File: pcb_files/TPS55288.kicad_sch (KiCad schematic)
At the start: 35 parts, among them Q6 CSD18513Q5A, Q7 CSD18513Q5A, U10 TPS55288RPMR

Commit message: Changed TPS55288 to internal droop compensation and added current monitoring for TPS55288 to ADC pin of LicheeRV Nano
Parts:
- removed C128: 4.7nF, Capacitor_SMD:C_0402_1005Metric, symbol JLCImport:CGA0402X7R472K250GT
- removed C134: 100nF, Capacitor_SMD:C_0402_1005Metric, symbol JLCImport:CL05B104KB54PNC
- removed R89: 56.2k, Resistor_SMD:R_0402_1005Metric, symbol JLCImport:0402WGF5622TCE
- removed R90: 42.2k, Resistor_SMD:R_0402_1005Metric, symbol JLCImport:CR0402F42K2Q10Z
- removed R91: 150k, Resistor_SMD:R_0603_1608Metric, symbol JLCImport:0603WAF1503T5E
- added C117: 10nF, Capacitor_SMD:C_0402_1005Metric, symbol JLCImport:TCC0402X7R103M500AT
- added C118: 4.7nF, Capacitor_SMD:C_0402_1005Metric, symbol JLCImport:TCC0402X7R472K500AT
- added R78: 56.2k, Resistor_SMD:R_0402_1005Metric, symbol JLCImport:CR0402FF5622G
- added R80: 20k, Resistor_SMD:R_0402_1005Metric, symbol JLCImport:CR0402J20K0Q10Z
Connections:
- net AGND: now also C117.1, C118.1, R80.1
- net I_MONITOR: now reaches U10.16 (CDC)
- net at U10.17 (ILIM): now also R80.2
- net at C127.2, U10.18 (COMP): now also R78.2
- net at U10.7 (DITH/SYNC): now also C117.2
- new net: C118.2, R78.1

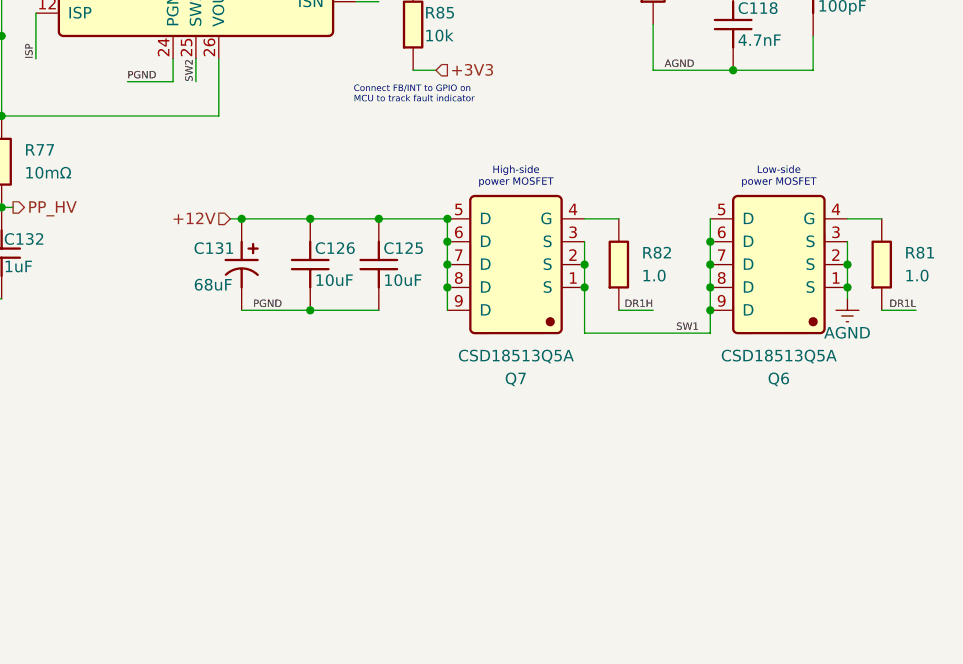
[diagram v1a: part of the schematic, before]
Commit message: Basic Function Review/Documentation for TPS55288
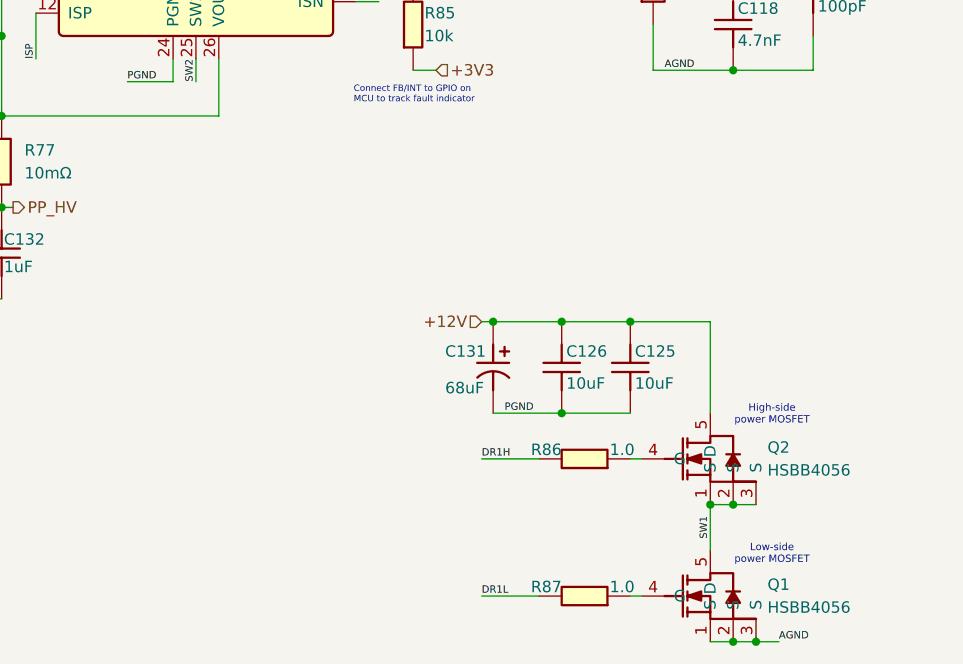
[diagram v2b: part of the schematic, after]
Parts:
- removed Q6, Q7: CSD18513Q5A, JLCImport:CSD18513Q5A, symbol JLCImport:CSD18513Q5A
- removed R81, R82: 1.0, Resistor_SMD:R_0402_1005Metric, symbol JLCImport:WR04W1R00FTL
- added Q1, Q2: HSBB4056, JLCImport:HSBB4056, symbol JLCImport:HSBB4056
- added R86, R87: 1.0, Resistor_SMD:R_0402_1005Metric, symbol JLCImport:WR04W1R00FTL
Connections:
- net +12V: now also Q2.5 (D)
- net DR1H: now also R86.2
- net DR1L: now also R87.2
- net SW1: now also Q1.5 (D), Q2.1 (S), Q2.2 (S), Q2.3 (S)
- net AGND renamed GND
- net GND: now also Q1.1 (S), Q1.2 (S), Q1.3 (S)
- new net: Q2.4 (G), R86.1
- new net: Q1.4 (G), R87.1

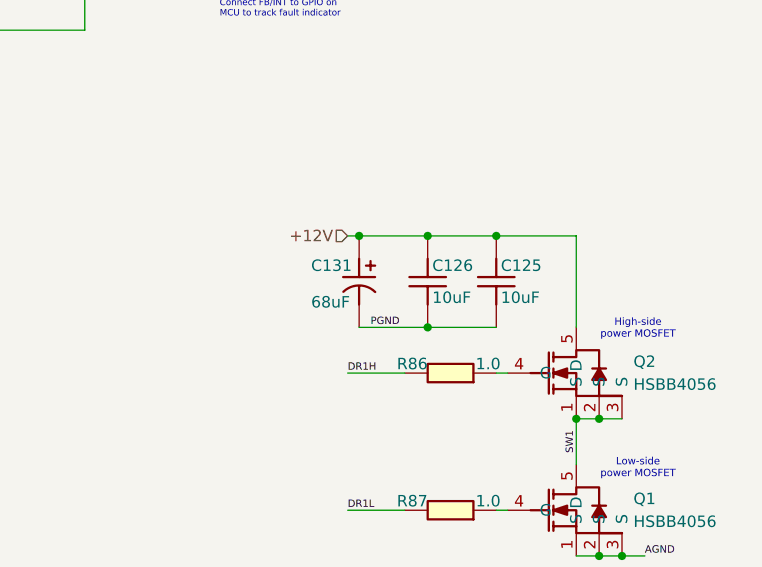
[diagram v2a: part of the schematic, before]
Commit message: Basic Function Review/Documentation for MCP9808
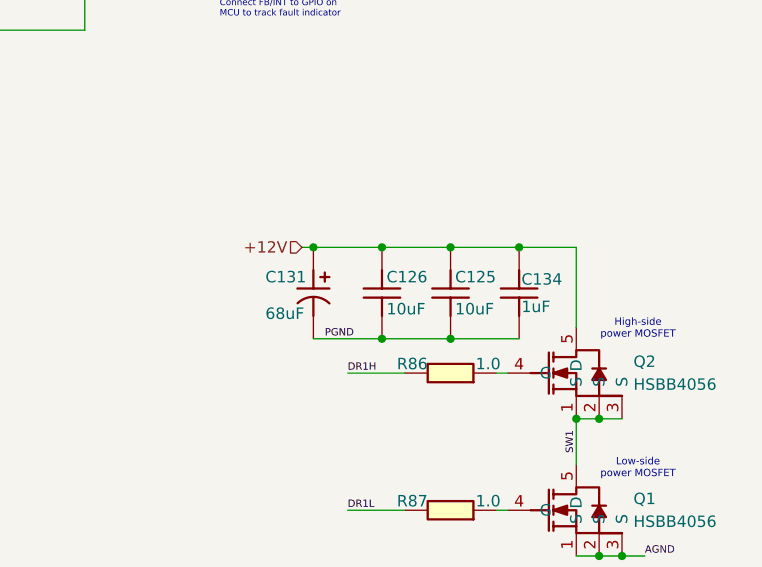
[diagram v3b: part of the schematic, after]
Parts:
- added C134: 1uF, Capacitor_SMD:C_0402_1005Metric, symbol JLCImport:CL05A105KA5NQNC
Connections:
- net +12V: now also C134.2
- net GND: now also C134.1
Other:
- moved on the sheet: C125, C126, C131
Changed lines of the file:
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@@
 	)
 	(junction
-		(at 154.94 109.22)
+		(at 149.86 110.49)
 		(diameter 0)
-		(color 0 0 0 0)
+		(color 139 0 0 1)
 	)
 	(junction
@@
 	)
 	(junction
-		(at 154.94 99.06)
+		(at 149.86 100.33)
 		(diameter 0)
 		(color 0 0 0 0)
@@
 	)
 	(junction
+		(at 157.48 110.49)
+		(diameter 0)
+		(color 139 0 0 1)
+	)
+	(junction
 		(at 60.96 57.15)
 		(diameter 0)
@@
 	)
 	(junction
-		(at 162.56 99.06)
+		(at 157.48 100.33)
 		(diameter 0)
 		(color 0 0 0 0)
@@
 	)
 	(junction
+		(at 165.1 100.33)
+		(diameter 0)
+		(color 0 0 0 0)
+	)
+	(junction
 		(at 74.93 53.34)
 		(diameter 0)
@@
 	)
 	(junction
-		(at 147.32 99.06)
+		(at 142.24 100.33)
 		(diameter 0)
 		(color 0 0 0 0)
@@
 	(wire
 		(pts
-			(xy 147.32 99.06) (xy 154.94 99.06)
+			(xy 142.24 100.33) (xy 149.86 100.33)
 		)
 		(stroke
@@
 	(wire
 		(pts
+			(xy 157.48 110.49) (xy 165.1 110.49)
+		)
+		(stroke
+			(width 0)
+			(type default)
+			(color 139 0 0 1)
+		)
+	)
+	(wire
+		(pts
 			(xy 149.86 40.64) (xy 151.13 40.64)
 		)
@@
 	(wire
 		(pts
-			(xy 74.93 53.34) (xy 74.93 52.07)
+			(xy 171.45 100.33) (xy 171.45 109.22)
 		)
 		(stroke
 			(width 0)
 			(type default)
-			(color 139 0 0 1)
 		)
 	)
 	(wire
 		(pts
-			(xy 31.75 58.42) (xy 31.75 57.15)
+			(xy 74.93 53.34) (xy 74.93 52.07)
 		)
 		(stroke
@@
 	(wire
 		(pts
-			(xy 165.1 71.12) (xy 173.99 71.12)
+			(xy 31.75 58.42) (xy 31.75 57.15)
 		)
 		(stroke
@@
 	(wire
 		(pts
-			(xy 171.45 109.22) (xy 171.45 99.06)
+			(xy 165.1 71.12) (xy 173.99 71.12)
 		)
 		(stroke
 			(width 0)
 			(type default)
+			(color 139 0 0 1)
 		)
 	)
@@
 	(wire
 		(pts
-			(xy 154.94 109.22) (xy 162.56 109.22)
+			(xy 149.86 110.49) (xy 157.48 110.49)
 		)
 		(stroke
@@
 	(wire
 		(pts
+			(xy 165.1 100.33) (xy 171.45 100.33)
+		)
+		(stroke
+			(width 0)
+			(type default)
+		)
+	)
+	(wire
+		(pts
 			(xy 173.99 134.62) (xy 176.53 134.62)
 		)
@@
 	(wire
 		(pts
-			(xy 162.56 99.06) (xy 171.45 99.06)
+			(xy 157.48 100.33) (xy 165.1 100.33)
 		)
 		(stroke
@@
 	(wire
 		(pts
-			(xy 147.32 109.22) (xy 154.94 109.22)
+			(xy 142.24 110.49) (xy 149.86 110.49)
 		)
 		(stroke
@@
 	(wire
 		(pts
-			(xy 154.94 99.06) (xy 162.56 99.06)
+			(xy 149.86 100.33) (xy 157.48 100.33)
 		)
 		(stroke
@@
 	(wire
 		(pts
-			(xy 146.05 99.06) (xy 147.32 99.06)
+			(xy 140.97 100.33) (xy 142.24 100.33)
 		)
 		(stroke
@@
 	)
 	(label "PGND"
-		(at 148.59 109.22 0)
+		(at 143.51 110.49 0)
 		(effects
 			(font
@@
 	(hierarchical_label "+12V"
 		(shape input)
-		(at 146.05 99.06 180)
+		(at 140.97 100.33 180)
 		(effects
 			(font
@@
 	(symbol
 		(lib_id "JLCImport:DHG100M686G150S1AA")
-		(at 147.32 104.14 270)
+		(at 142.24 105.41 270)
 		(unit 1)
 		(body_style 1)
@@
 		(dnp no)
 		(property "Reference" "C131"
-			(at 141.986 102.362 90)
+			(at 136.906 103.632 90)
 			(show_name no)
 			(do_not_autoplace no)
@@
 		)
 		(property "Value" "68uF"
-			(at 141.986 106.426 90)
+			(at 136.906 107.696 90)
 			(show_name no)
 			(do_not_autoplace no)
@@
 		)
 		(property "Footprint" "JLCImport:DHG100M686G150S1AA"
-			(at 147.32 104.14 0)
+			(at 142.24 105.41 0)
 			(hide yes)
 			(show_name no)
@@
 		)
 		(property "Datasheet" "https://atta.szlcsc.com/upload/public/pdf/source/20250828/0654BD1517550F7FB040F38784C4EB35.pdf"
-			(at 147.32 104.14 0)
+			(at 142.24 105.41 0)
 			(hide yes)
 			(show_name no)
@@
 		)
 		(property "Description" "68uF ±20% 100V"
-			(at 147.32 104.14 0)
+			(at 142.24 105.41 0)
 			(hide yes)
 			(show_name no)
@@
 		)
 		(property "LCSC" "C46551229"
-			(at 147.32 104.14 0)
+			(at 142.24 105.41 0)
 			(hide yes)
 			(show_name no)
@@
 		)
 		(property "Manufacturer" "KNSCHA(科尼盛)"
-			(at 147.32 104.14 0)
+			(at 142.24 105.41 0)
 			(hide yes)
 			(show_name no)
@@
 		)
 		(property "Manufacturer Part" "DHG100M686G150S1AA"
-			(at 147.32 104.14 0)
+			(at 142.24 105.41 0)
 			(hide yes)
 			(show_name no)
@@
 		(lib_name "CL21A106KAYNNNE_1")
 		(lib_id "JLCImport:CL21A106KAYNNNE")
-		(at 162.56 104.14 90)
+		(at 157.48 105.41 90)
 		(unit 1)
 		(body_style 1)
@@
 		(dnp no)
 		(property "Reference" "C125"
-			(at 163.068 102.362 90)
+			(at 157.988 103.632 90)
 			(show_name no)
 			(do_not_autoplace no)
@@
 		)
 		(property "Value" "10uF"
-			(at 163.068 105.918 90)
+			(at 157.988 107.188 90)
 			(show_name no)
 			(do_not_autoplace no)
@@
 		)
 		(property "Footprint" "Capacitor_SMD:C_0805_2012Metric"
-			(at 162.56 104.14 0)
+			(at 157.48 105.41 0)
 			(hide yes)
 			(show_name no)
@@
 		)
 		(property "Datasheet" "https://www.lcsc.com/datasheet/lcsc_datasheet_2304140030_Samsung-Electro-Mechanics-CL21A106KAYNNNE_C15850.pdf"
-			(at 162.56 104.14 0)
+			(at 157.48 105.41 0)
 			(hide yes)
 			(show_name no)
@@
 		)
 		(property "Description" "10uF 25V X5R ±10% 0805 Multilayer Ceramic Capacitors MLCC - SMD/SMT ROHS"
-			(at 162.56 104.14 0)
+			(at 157.48 105.41 0)
 			(hide yes)
 			(show_name no)
@@
 		)
 		(property "LCSC" "C15850"
-			(at 162.56 104.14 0)
+			(at 157.48 105.41 0)
 			(hide yes)
 			(show_name no)
@@
 		)
 		(property "Manufacturer" "Samsung Electro-Mechanics"
-			(at 162.56 104.14 0)
+			(at 157.48 105.41 0)
 			(hide yes)
 			(show_name no)
@@
 		)
 		(property "Manufacturer Part" "CL21A106KAYNNNE"
-			(at 162.56 104.14 0)
+			(at 157.48 105.41 0)
 			(hide yes)
 			(show_name no)
@@
 		(lib_name "CL21A106KAYNNNE_1")
 		(lib_id "JLCImport:CL21A106KAYNNNE")
-		(at 154.94 104.14 90)
+		(at 149.86 105.41 90)
 		(unit 1)
 		(body_style 1)
@@
 		(dnp no)
 		(property "Reference" "C126"
-			(at 155.448 102.362 90)
+			(at 150.368 103.632 90)
 			(show_name no)
 			(do_not_autoplace no)
@@
 		)
 		(property "Value" "10uF"
-			(at 155.448 105.918 90)
+			(at 150.368 107.188 90)
 			(show_name no)
 			(do_not_autoplace no)
@@
 		)
 		(property "Footprint" "Capacitor_SMD:C_0805_2012Metric"
-			(at 154.94 104.14 0)
+			(at 149.86 105.41 0)
 			(hide yes)
 			(show_name no)
@@
 		)
 		(property "Datasheet" "https://www.lcsc.com/datasheet/lcsc_datasheet_2304140030_Samsung-Electro-Mechanics-CL21A106KAYNNNE_C15850.pdf"
-			(at 154.94 104.14 0)
+			(at 149.86 105.41 0)
 			(hide yes)
 			(show_name no)
@@
 		)
 		(property "Description" "10uF 25V X5R ±10% 0805 Multilayer Ceramic Capacitors MLCC - SMD/SMT ROHS"
-			(at 154.94 104.14 0)
+			(at 149.86 105.41 0)
 			(hide yes)
 			(show_name no)
@@
 		)
 		(property "LCSC" "C15850"
-			(at 154.94 104.14 0)
+			(at 149.86 105.41 0)
 			(hide yes)
 			(show_name no)
@@
 		)
 		(property "Manufacturer" "Samsung Electro-Mechanics"
-			(at 154.94 104.14 0)
+			(at 149.86 105.41 0)
 			(hide yes)
 			(show_name no)
@@
 		)
 		(property "Manufacturer Part" "CL21A106KAYNNNE"
-			(at 154.94 104.14 0)
+			(at 149.86 105.41 0)
 			(hide yes)
 			(show_name no)
@@
 					(unit 1)
 				)
+			)
+		)
+	)
+	(symbol
+		(lib_id "JLCImport:CL05A105KA5NQNC")
+		(at 165.1 105.41 90)
+		(unit 1)
+		(body_style 1)
+		(exclude_from_sim no)
+		(in_bom yes)
+		(on_board yes)
+		(in_pos_files yes)
+		(dnp no)
+		(property "Reference" "C134"
+			(at 165.354 103.886 90)
+			(show_name no)
+			(do_not_autoplace no)
+			(effects
+				(font
+					(size 1.27 1.27)
+				)
+				(justify right)
+			)
+		)
+		(property "Value" "1uF"
+			(at 165.354 106.934 90)
+			(show_name no)
+			(do_not_autoplace no)
+			(effects
+				(font
+					(size 1.27 1.27)
+				)
+				(justify right)
+			)
+		)
+		(property "Footprint" "Capacitor_SMD:C_0402_1005Metric"
+			(at 165.1 105.41 0)
+			(hide yes)
+			(show_name no)
+			(do_not_autoplace no)
+			(effects
+				(font
+					(size 1.27 1.27)
+				)
+			)
+		)
+		(property "Datasheet" "https://www.lcsc.com/datasheet/lcsc_datasheet_2304140030_Samsung-Electro-Mechanics-CL05A105KA5NQNC_C52923.pdf"
+			(at 165.1 105.41 0)
+			(hide yes)
+			(show_name no)
+			(do_not_autoplace no)
+			(effects
+				(font
+					(size 1.27 1.27)
+				)
+			)
+		)
+		(property "Description" "1uF 25V X5R ±10% 0402 Multilayer Ceramic Capacitors MLCC - SMD/SMT ROHS"
+			(at 165.1 105.41 0)
+			(hide yes)
+			(show_name no)
+			(do_not_autoplace no)
+			(effects
+				(font
+					(size 1.27 1.27)
+				)
+			)
+		)
+		(property "LCSC" "C52923"
+			(at 165.1 105.41 0)
+			(hide yes)
+			(show_name no)
+			(do_not_autoplace no)
+			(effects
+				(font
+					(size 1.27 1.27)
+				)
+			)
+		)
+		(property "Manufacturer" "Samsung Electro-Mechanics"
+			(at 165.1 105.41 0)
+			(hide yes)
+			(show_name no)
+			(do_not_autoplace no)
+			(effects
+				(font
+					(size 1.27 1.27)
+				)
+			)
+		)
+		(property "Manufacturer Part" "CL05A105KA5NQNC"
+			(at 165.1 105.41 0)
+			(hide yes)
+			(show_name no)
+			(do_not_autoplace no)
+			(effects
+				(font
+					(size 1.27 1.27)
+				)
+			)
+		)
+		(pin "2"
+		)
+		(pin "1"
+		)
+		(instances
+			(project "serverv2_backplane"
+				(path "/d38d6818-cf53-410d-afa3-a75a85b7c05a/b43497c2-ce72-4a73-863d-5d490b2b70e6"
+					(reference "C134")
+					(unit 1)
+				)
